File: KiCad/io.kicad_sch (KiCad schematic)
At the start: 77 parts, among them Q401 BC857W, Q402 BC857W, Q403 BC857W, Q404 BC857W, Q405 BC857W, SW401 SW_DIP_x04, SW402 SW_DIP_x04, SW403 SW_Omron_B3FS, SW404 SW_Omron_B3FS, SW405 SW_Omron_B3FS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

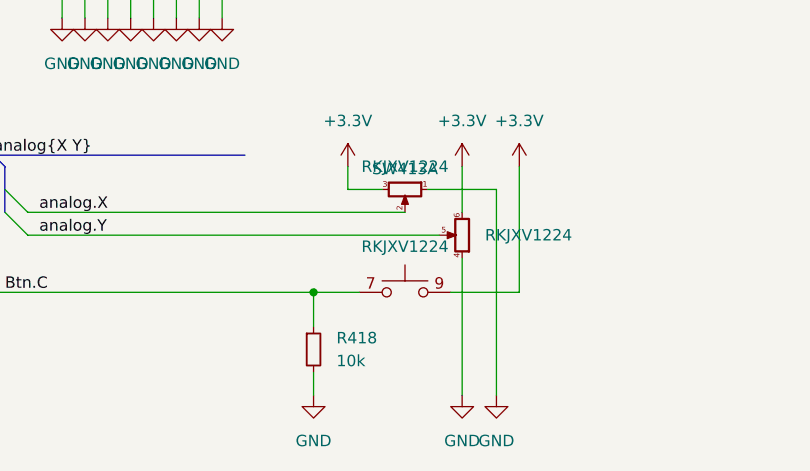
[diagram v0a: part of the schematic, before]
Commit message: replaced SAR-ADC with Sigma-Delta-Converter
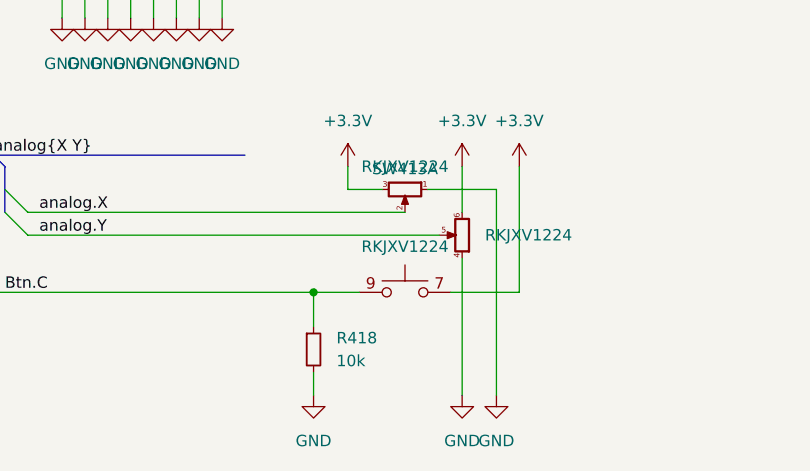
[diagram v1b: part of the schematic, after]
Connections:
- net +3.3V: now also SW413.7 (A), SW413.8 (A); no longer SW413.10 (B), SW413.9 (B)
- net Btn.C: now also SW413.10 (B), SW413.9 (B); no longer SW413.7 (A), SW413.8 (A)
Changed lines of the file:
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@@
 		(lib_id "FPGA-Devel:RKJXV1224")
 		(at 81.28 171.45 0)
+		(mirror y)
 		(unit 3)
 		(exclude_from_sim no)

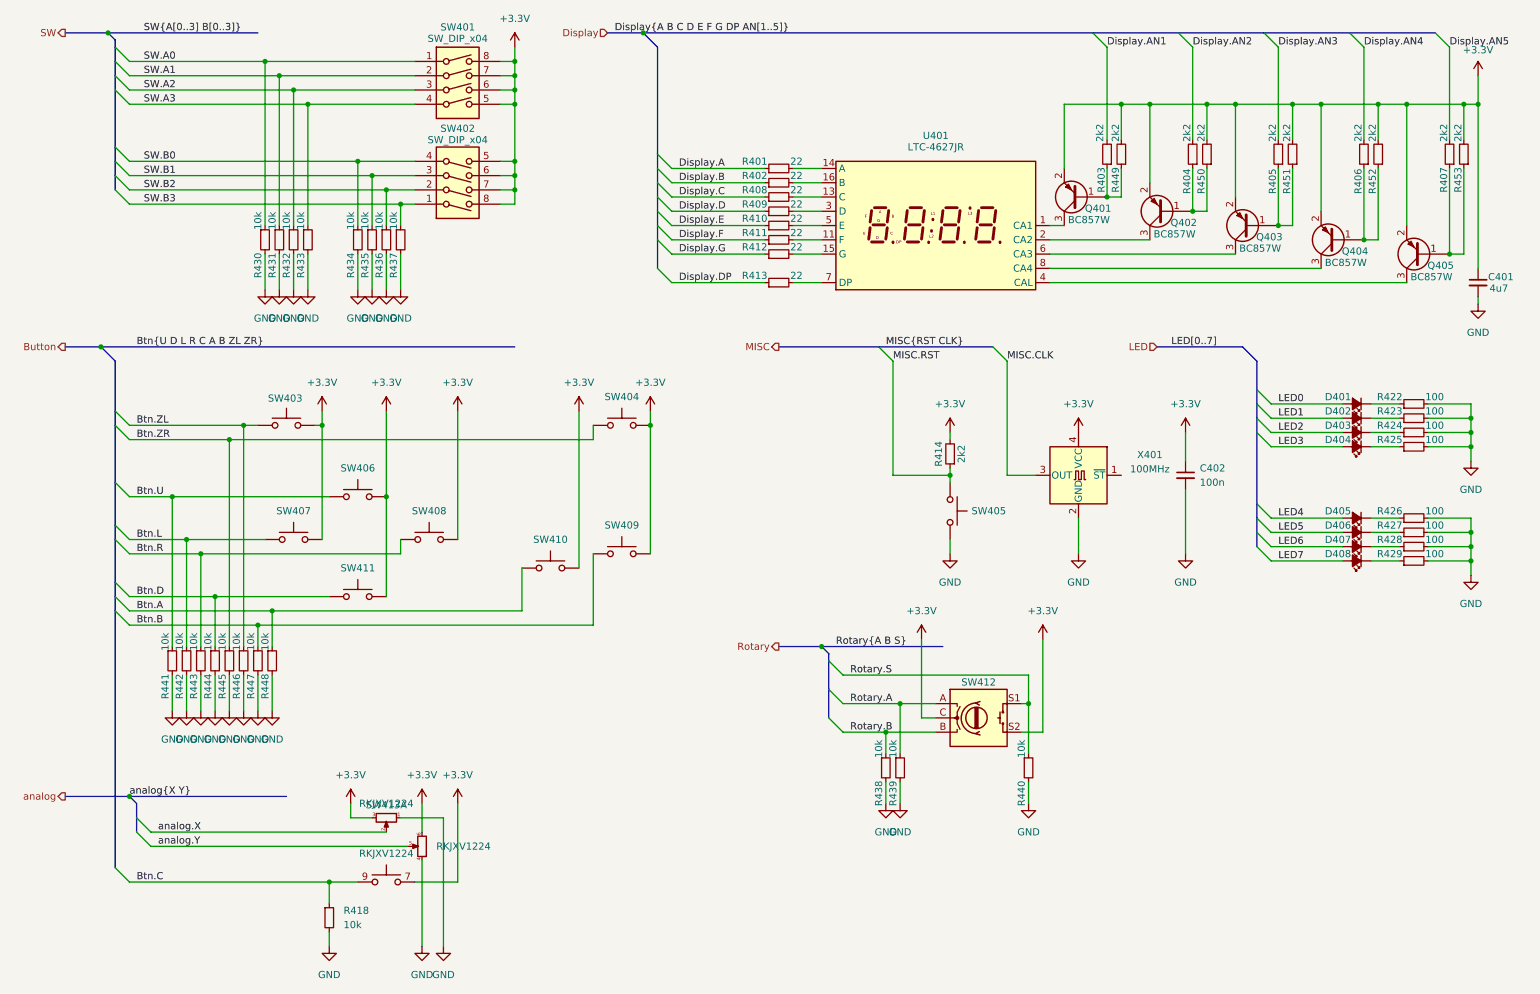
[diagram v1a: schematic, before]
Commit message: Vorberitung für micro-SD
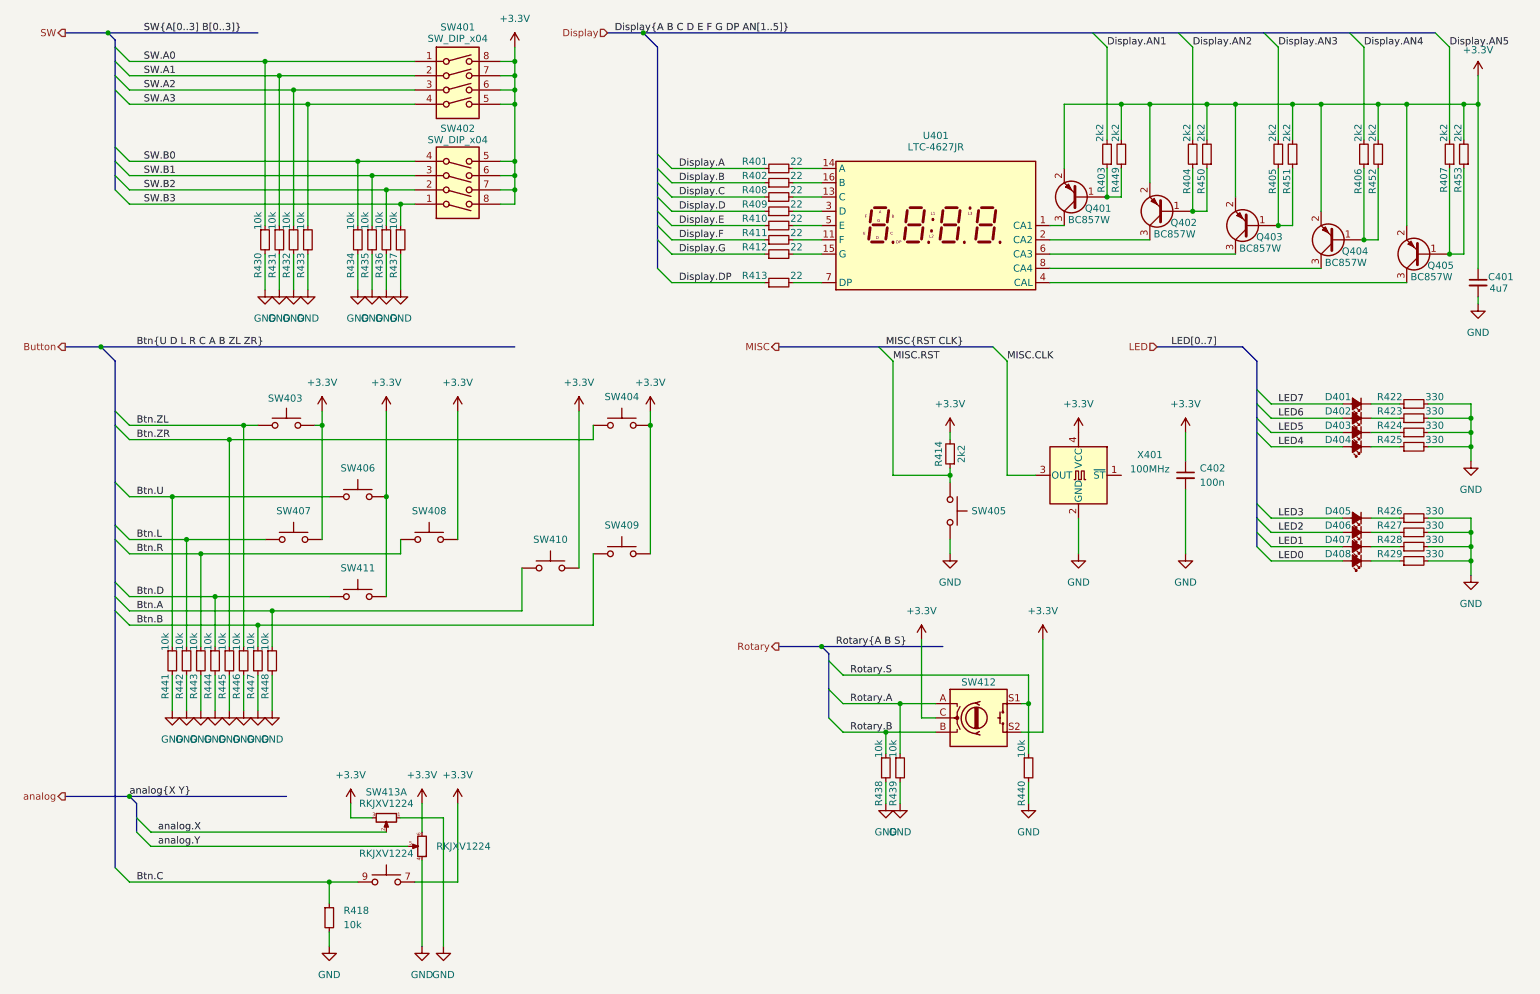
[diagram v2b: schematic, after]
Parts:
- R422, R423, R424, R425, R426, R427, R428, R429: value 100 -> 330; Würth 560112110022 -> 560112110231
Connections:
- net +3.3V: now also SW404.1; no longer SW404.2
- net Btn.ZR: now also SW404.2; no longer SW404.1
- net LED0: now also D408.2 (A); no longer D401.2 (A)
- net LED1: now also D407.2 (A); no longer D402.2 (A)
- net LED2: now also D406.2 (A); no longer D403.2 (A)
- net LED3: now also D405.2 (A); no longer D404.2 (A)
- net LED4: now also D404.2 (A); no longer D405.2 (A)
- net LED5: now also D403.2 (A); no longer D406.2 (A)
- net LED6: now also D402.2 (A); no longer D407.2 (A)
- net LED7: now also D401.2 (A); no longer D408.2 (A)
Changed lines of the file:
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@@
 	)
 	(label "LED5"
-		(at 240.03 109.22 0)
+		(at 240.03 91.44 0)
 		(effects
 			(font
@@
 	)
 	(label "LED0"
-		(at 240.03 86.36 0)
+		(at 240.03 114.3 0)
 		(effects
 			(font
@@
 	)
 	(label "LED2"
-		(at 240.03 91.44 0)
+		(at 240.03 109.22 0)
 		(effects
 			(font
@@
 	)
 	(label "LED7"
-		(at 240.03 114.3 0)
+		(at 240.03 86.36 0)
 		(effects
 			(font
@@
 	)
 	(label "LED1"
-		(at 240.03 88.9 0)
+		(at 240.03 111.76 0)
 		(effects
 			(font
@@
 	)
 	(label "LED6"
-		(at 240.03 111.76 0)
+		(at 240.03 88.9 0)
 		(effects
 			(font
@@
 	)
 	(label "LED3"
-		(at 240.03 93.98 0)
+		(at 240.03 106.68 0)
 		(effects
 			(font
@@
 	)
 	(label "LED4"
-		(at 240.03 106.68 0)
+		(at 240.03 93.98 0)
 		(effects
 			(font
@@
 		(dnp no)
 		(property "Reference" "SW413"
-			(at 81.28 157.734 90)
+			(at 81.28 155.448 90)
 			(effects
 				(font
@@
 		(lib_id "Switch:SW_Omron_B3FS")
 		(at 123.19 90.17 0)
+		(mirror y)
 		(unit 1)
 		(exclude_from_sim no)
@@
 		(on_board yes)
 		(dnp no)
-		(fields_autoplaced yes)
 		(property "Reference" "SW404"
 			(at 123.19 85.09 0)
@@
 			)
 		)
-		(property "Value" "100"
+		(property "Value" "330"
 			(at 266.192 88.392 90)
 			(effects
@@
 			)
 		)
-		(property "Würth" "560112110022"
+		(property "Würth" "560112110231"
 			(at 264.16 88.9 0)
 			(effects
@@
 			)
 		)
-		(property "Value" "100"
+		(property "Value" "330"
 			(at 266.192 108.712 90)
 			(effects
@@
 			)
 		)
-		(property "Würth" "560112110022"
+		(property "Würth" "560112110231"
 			(at 264.16 109.22 0)
 			(effects
@@
 			)
 		)
-		(property "Value" "100"
+		(property "Value" "330"
 			(at 266.192 113.792 90)
 			(effects
@@
 			)
 		)
-		(property "Würth" "560112110022"
+		(property "Würth" "560112110231"
 			(at 264.16 114.3 0)
 			(effects
@@
 			)
 		)
-		(property "Value" "100"
+		(property "Value" "330"
 			(at 266.192 111.252 90)
 			(effects
@@
 			)
 		)
-		(property "Würth" "560112110022"
+		(property "Würth" "560112110231"
 			(at 264.16 111.76 0)
 			(effects
@@
 			)
 		)
-		(property "Value" "100"
+		(property "Value" "330"
 			(at 266.192 93.472 90)
 			(effects
@@
 			)
 		)
-		(property "Würth" "560112110022"
+		(property "Würth" "560112110231"
 			(at 264.16 93.98 0)
 			(effects
@@
 			)
 		)
-		(property "Value" "100"
+		(property "Value" "330"
 			(at 266.192 106.172 90)
 			(effects
@@
 			)
 		)
-		(property "Würth" "560112110022"
+		(property "Würth" "560112110231"
 			(at 264.16 106.68 0)
 			(effects
@@
 			)
 		)
-		(property "Value" "100"
+		(property "Value" "330"
 			(at 266.192 90.932 90)
 			(effects
@@
 			)
 		)
-		(property "Würth" "560112110022"
+		(property "Würth" "560112110231"
 			(at 264.16 91.44 0)
 			(effects
@@
 			)
 		)
-		(property "Value" "100"
+		(property "Value" "330"
 			(at 266.192 85.852 90)
 			(effects
@@
 			)
 		)
-		(property "Würth" "560112110022"
+		(property "Würth" "560112110231"
 			(at 264.16 86.36 0)
 			(effects

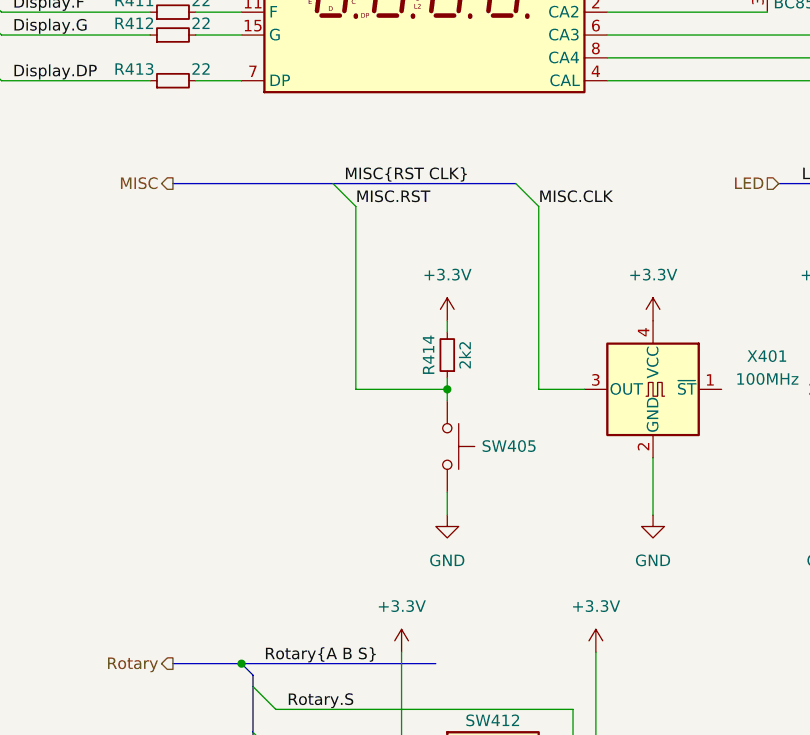
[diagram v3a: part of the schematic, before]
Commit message: LEDs zur Visualisierung des ausgewählten FPGAs
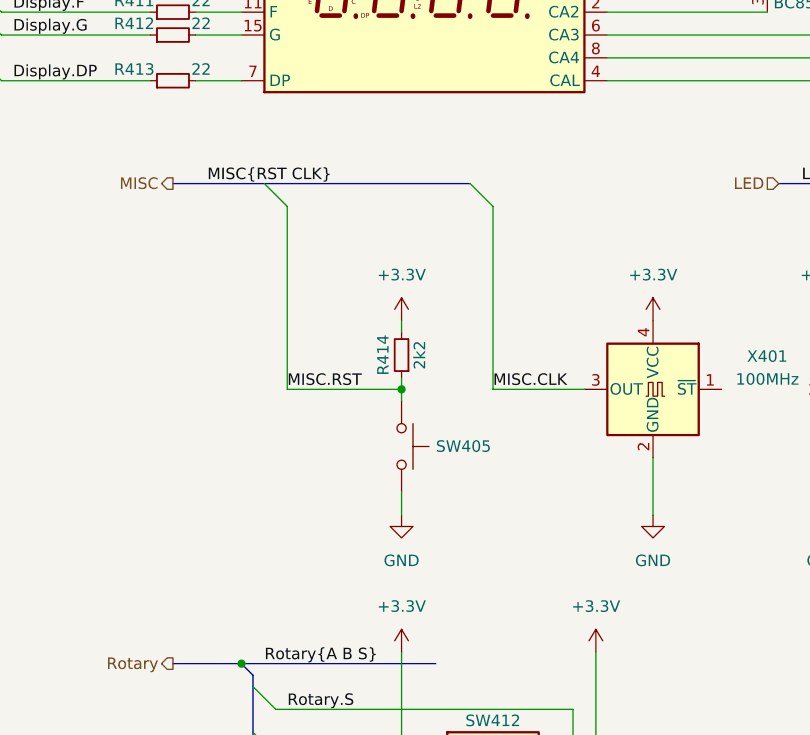
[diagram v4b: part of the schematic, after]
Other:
- moved on the sheet: R414, SW405
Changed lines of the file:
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@@
 	)
 	(junction
-		(at 181.61 99.06)
+		(at 176.53 99.06)
 		(diameter 0)
 		(color 0 0 0 0)
@@
 	)
 	(bus_entry
-		(at 189.23 76.2)
+		(at 184.15 76.2)
 		(size 2.54 2.54)
 		(stroke
@@
 	)
 	(bus_entry
-		(at 168.91 76.2)
+		(at 161.29 76.2)
 		(size 2.54 2.54)
 		(stroke
@@
 	(bus
 		(pts
-			(xy 151.13 76.2) (xy 168.91 76.2)
+			(xy 151.13 76.2) (xy 184.15 76.2)
 		)
 		(stroke
@@
 	(bus
 		(pts
-			(xy 168.91 76.2) (xy 189.23 76.2)
-		)
-		(stroke
-			(width 0)
-			(type default)
-		)
-	)
-	(bus
-		(pts
 			(xy 236.22 86.36) (xy 236.22 88.9)
 		)
@@
 	(wire
 		(pts
-			(xy 191.77 78.74) (xy 191.77 99.06)
+			(xy 186.69 78.74) (xy 186.69 99.06)
 		)
 		(stroke
@@
 	(wire
 		(pts
-			(xy 181.61 110.49) (xy 181.61 113.03)
+			(xy 176.53 110.49) (xy 176.53 113.03)
 		)
 		(stroke
@@
 	(wire
 		(pts
-			(xy 181.61 97.79) (xy 181.61 99.06)
+			(xy 176.53 97.79) (xy 176.53 99.06)
 		)
 		(stroke
@@
 	(wire
 		(pts
-			(xy 171.45 78.74) (xy 171.45 99.06)
+			(xy 163.83 78.74) (xy 163.83 99.06)
 		)
 		(stroke
@@
 	(wire
 		(pts
-			(xy 181.61 91.44) (xy 181.61 92.71)
+			(xy 176.53 91.44) (xy 176.53 92.71)
 		)
 		(stroke
@@
 	(wire
 		(pts
-			(xy 191.77 99.06) (xy 196.85 99.06)
+			(xy 186.69 99.06) (xy 196.85 99.06)
 		)
 		(stroke
@@
 	(wire
 		(pts
-			(xy 181.61 99.06) (xy 181.61 100.33)
+			(xy 176.53 99.06) (xy 176.53 100.33)
 		)
 		(stroke
@@
 	(wire
 		(pts
-			(xy 171.45 99.06) (xy 181.61 99.06)
+			(xy 163.83 99.06) (xy 176.53 99.06)
 		)
 		(stroke
@@
 	)
 	(label "MISC{RST CLK}"
-		(at 170.18 76.2 0)
+		(at 154.94 76.2 0)
 		(effects
 			(font
@@
 	)
 	(label "MISC.CLK"
-		(at 191.77 78.74 0)
+		(at 186.69 99.06 0)
 		(effects
 			(font
@@
 	)
 	(label "MISC.RST"
-		(at 171.45 78.74 0)
+		(at 163.83 99.06 0)
 		(effects
 			(font
@@
 	(symbol
 		(lib_id "Switch:SW_Omron_B3FS")
-		(at 181.61 105.41 270)
+		(at 176.53 105.41 270)
 		(unit 1)
 		(body_style 1)
@@
 		(fields_autoplaced yes)
 		(property "Reference" "SW405"
-			(at 185.42 105.4099 90)
+			(at 180.34 105.4099 90)
 			(show_name no)
 			(do_not_autoplace no)
@@
 		)
 		(property "Value" "SW_Omron_B3FS"
-			(at 186.69 105.41 0)
+			(at 181.61 105.41 0)
 			(hide yes)
 			(show_name no)
@@
 		)
 		(property "Footprint" "Library:SW_PUSH_6mm_H4.3mm"
-			(at 186.69 105.41 0)
+			(at 181.61 105.41 0)
 			(hide yes)
 			(show_name no)
@@
 		)
 		(property "Datasheet" "https://omronfs.omron.com/en_US/ecb/products/pdf/en-b3fs.pdf"
-			(at 186.69 105.41 0)
+			(at 181.61 105.41 0)
 			(hide yes)
 			(show_name no)
@@
 		)
 		(property "Description" "Omron B3FS 6x6mm single pole normally-open tactile switch"
-			(at 181.61 105.41 0)
+			(at 176.53 105.41 0)
 			(hide yes)
 			(show_name no)
@@
 		)
 		(property "Würth" "430156043736"
-			(at 181.61 105.41 0)
+			(at 176.53 105.41 0)
 			(hide yes)
 			(show_name no)
@@
 	(symbol
 		(lib_id "power:GND")
-		(at 181.61 113.03 0)
+		(at 176.53 113.03 0)
 		(unit 1)
 		(body_style 1)
@@
 		(fields_autoplaced yes)
 		(property "Reference" "#PWR0428"
-			(at 181.61 119.38 0)
+			(at 176.53 119.38 0)
 			(hide yes)
 			(show_name no)
@@
 		)
 		(property "Value" "GND"
-			(at 181.61 118.11 0)
+			(at 176.53 118.11 0)
 			(show_name no)
 			(do_not_autoplace no)
@@
 		)
 		(property "Footprint" ""
-			(at 181.61 113.03 0)
+			(at 176.53 113.03 0)
 			(hide yes)
 			(show_name no)
@@
 		)
 		(property "Datasheet" ""
-			(at 181.61 113.03 0)
+			(at 176.53 113.03 0)
 			(hide yes)
 			(show_name no)
@@
 		)
 		(property "Description" "Power symbol creates a global label with name \"GND\" , ground"
-			(at 181.61 113.03 0)
+			(at 176.53 113.03 0)
 			(hide yes)
 			(show_name no)
@@
 	(symbol
 		(lib_id "power:+3.3V")
-		(at 181.61 91.44 0)
+		(at 176.53 91.44 0)
 		(unit 1)
 		(body_style 1)
@@
 		(fields_autoplaced yes)
 		(property "Reference" "#PWR0423"
-			(at 181.61 95.25 0)
+			(at 176.53 95.25 0)
 			(hide yes)
 			(show_name no)
@@
 		)
 		(property "Value" "+3.3V"
-			(at 181.61 86.36 0)
+			(at 176.53 86.36 0)
 			(show_name no)
 			(do_not_autoplace no)
@@
 		)
 		(property "Footprint" ""
-			(at 181.61 91.44 0)
+			(at 176.53 91.44 0)
 			(hide yes)
 			(show_name no)
@@
 		)
 		(property "Datasheet" ""
-			(at 181.61 91.44 0)
+			(at 176.53 91.44 0)
 			(hide yes)
 			(show_name no)
@@
 		)
 		(property "Description" "Power symbol creates a global label with name \"+3.3V\""
-			(at 181.61 91.44 0)
+			(at 176.53 91.44 0)
 			(hide yes)
 			(show_name no)
@@
 	(symbol
 		(lib_id "Device:R_Small")
-		(at 181.61 95.25 180)
+		(at 176.53 95.25 180)
 		(unit 1)
 		(body_style 1)
@@
 		(dnp no)
 		(property "Reference" "R414"
-			(at 179.578 95.25 90)
+			(at 174.498 95.25 90)
 			(show_name no)
 			(do_not_autoplace no)
@@
 		)
 		(property "Value" "2k2"
-			(at 183.642 95.25 90)
+			(at 178.562 95.25 90)
 			(show_name no)
 			(do_not_autoplace no)
@@
 		)
 		(property "Footprint" "Resistor_SMD:R_0402_1005Metric"
-			(at 181.61 95.25 0)
+			(at 176.53 95.25 0)
 			(hide yes)
 			(show_name no)
@@
 		)
 		(property "Datasheet" ""
-			(at 181.61 95.25 0)
+			(at 176.53 95.25 0)
 			(hide yes)
 			(show_name no)
@@
 		)
 		(property "Description" "Resistor, small symbol"
-			(at 181.61 95.25 0)
+			(at 176.53 95.25 0)
 			(hide yes)
 			(show_name no)
@@
 		)
 		(property "Würth" "560112110087"
-			(at 181.61 95.25 0)
+			(at 176.53 95.25 0)
 			(hide yes)
 			(show_name no)
